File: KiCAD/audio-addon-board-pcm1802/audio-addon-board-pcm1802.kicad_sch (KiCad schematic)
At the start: 68 parts, among them J1 RCA, J2 CONN_HOST_1, J3 RCA, J4 RCA, J5 RCA, SW1 SW_DIP_x04, U1 PCM1802DBR, U2 LTC1682IS8-5, U3 SN74LVC1G125DBV

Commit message: working on layout
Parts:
- added C25: 1uF, Capacitor_SMD:C_0603_1608Metric, symbol Device:C_Small
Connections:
- net +3.3V: now also C25.2
- net GND: now also J1.2 (Ext), J4.2 (Ext), C25.1
- net VINL: now also SW1.7; no longer SW1.8
- net VINR: now also SW1.6; no longer SW1.5
- net at SW1.1: now also C12.2, RA3.1; no longer C20.1
- net at C17.2, RA4.1: now also SW1.4; no longer SW1.3
- net at C21.1: now also SW1.3; no longer SW1.4
- net at RA2.1, RA4.2: now also SW1.5; no longer SW1.6
- net at RA1.1, RA3.2: now also SW1.8; no longer SW1.7
- new net: C20.1, SW1.2

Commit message: working on layout (2025-10-09 sent to jlc)
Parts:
- C1, C10, C15, C22, C3, C5, C6, C9, CNP1: LCSC PN (none) -> C96446
- C11, C13, C14, C16, C2, C7, C8, CNP2: LCSC PN (none) -> C21120
- C12, C17, C23, C24, C25: LCSC PN (none) -> C15849
- C18, C19: LCSC PN (none) -> C14858
- C20, C21: LCSC PN (none) -> C53987
- C4: LCSC PN (none) -> C1588
- FB1: LCSC PN (none) -> C1017
- J1, J3, J4, J5, R12, RBYPASS1, RFMT0, RFMT1, RMODE0, RMODE1, ROSR1: now not fitted
- R1, R2, R22: LCSC PN (none) -> C22936
- R10, R5, R6, R7: LCSC PN (none) -> C23345
- R11, R13, R14, R9, RA1, RA2: LCSC PN (none) -> C21190
- R3, R4, R8, RBYPASS2, RFMT2, RFMT4, RMODE2, RMODE4, ROSR2: LCSC PN (none) -> C21189
- RA3, RA4: LCSC PN (none) -> C25819
- SW1: LCSC PN (none) -> C319050
- TP1: footprint TestPoint:TestPoint_Pad_2.0x2.0mm -> TestPoint:TestPoint_Pad_D1.5mm; now not fitted
- U1: LCSC PN (none) -> C1520787
- U2: LCSC PN (none) -> C676404
- U3: LCSC PN (none) -> C23654
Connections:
- net at C24.2, R13.2, R9.1: now also J2.4 (Pin_4); no longer J2.6 (Pin_6)
- net at C23.2, R11.2, R14.1: now also J2.1 (Pin_1); no longer J2.4 (Pin_4)

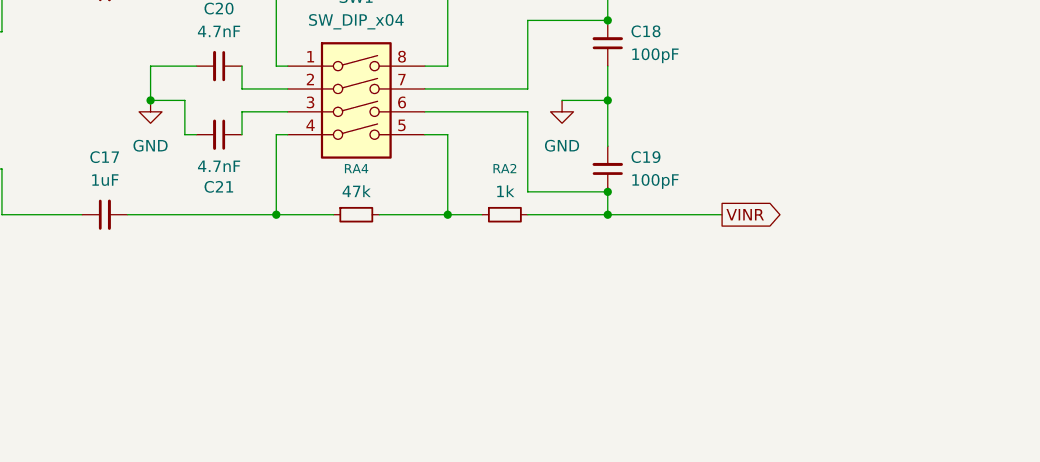
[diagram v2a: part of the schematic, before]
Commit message: add note to fix cap values
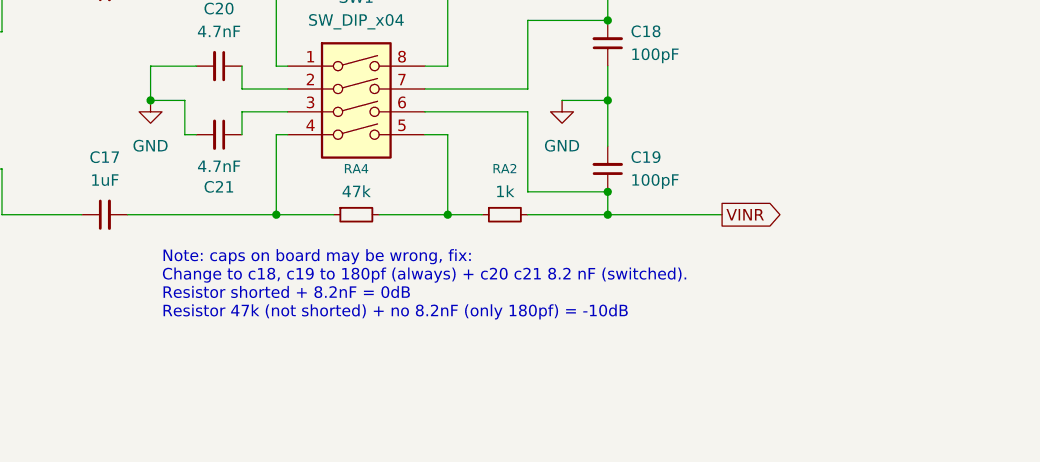
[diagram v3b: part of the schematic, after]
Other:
- note added: "Note: caps on board may be wrong, fix: Change to c18, c19 to 180pf (always) + c20 c21 8.2 nF (switched). Resistor shorted + 8.2nF = 0dB Resistor 47k (not shorted) + no 8.2nF (only 180pf) = -10dB"
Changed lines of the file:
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@@
 	(generator_version "9.0")
 	(paper "A3")
+	(text "Note: caps on board may be wrong, fix:\nChange to c18, c19 to 180pf (always) + c20 c21 8.2 nF (switched).\nResistor shorted + 8.2nF = 0dB\nResistor 47k (not shorted) + no 8.2nF (only 180pf) = -10dB"
+		(exclude_from_sim no)
+		(at 240.03 172.974 0)
+		(effects
+			(font
+				(size 1.27 1.27)
+			)
+			(justify left)
+		)
+	)
 	(text "SCKI, BCK, LRCK, FSYNC, DOUT all 22R"
 		(exclude_from_sim no)
@@
 		(on_board yes)
 		(dnp no)
-		(fields_autoplaced yes)
 		(property "Reference" "C20"
 			(at 246.3736 142.24 90)
@@
 		(on_board yes)
 		(dnp no)
-		(fields_autoplaced yes)
 		(property "Reference" "C17"
 			(at 233.6863 158.75 90)

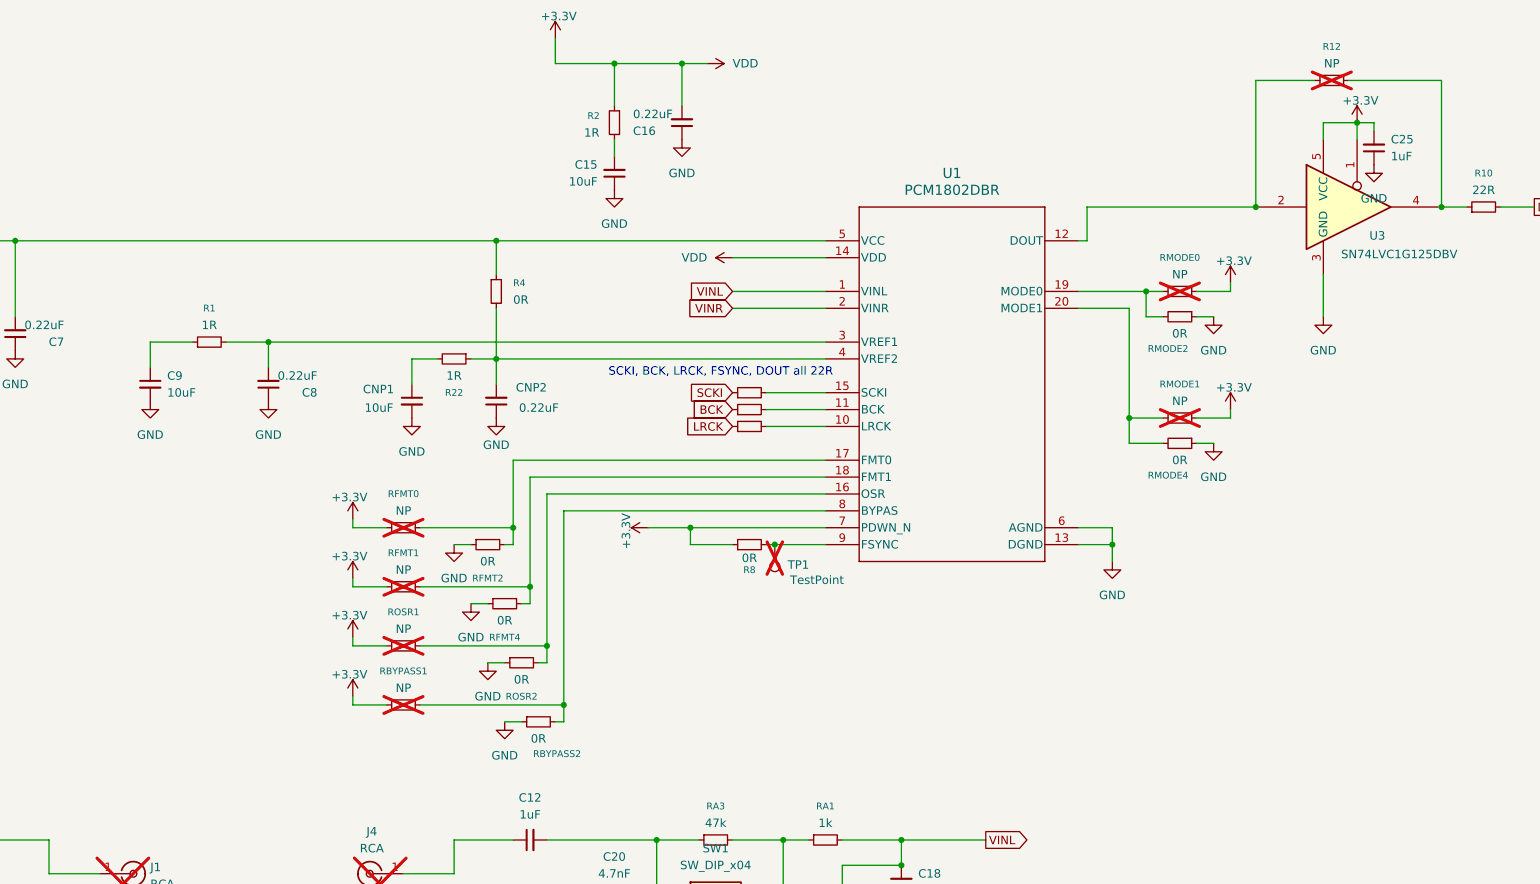
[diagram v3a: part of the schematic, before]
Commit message: update schematic
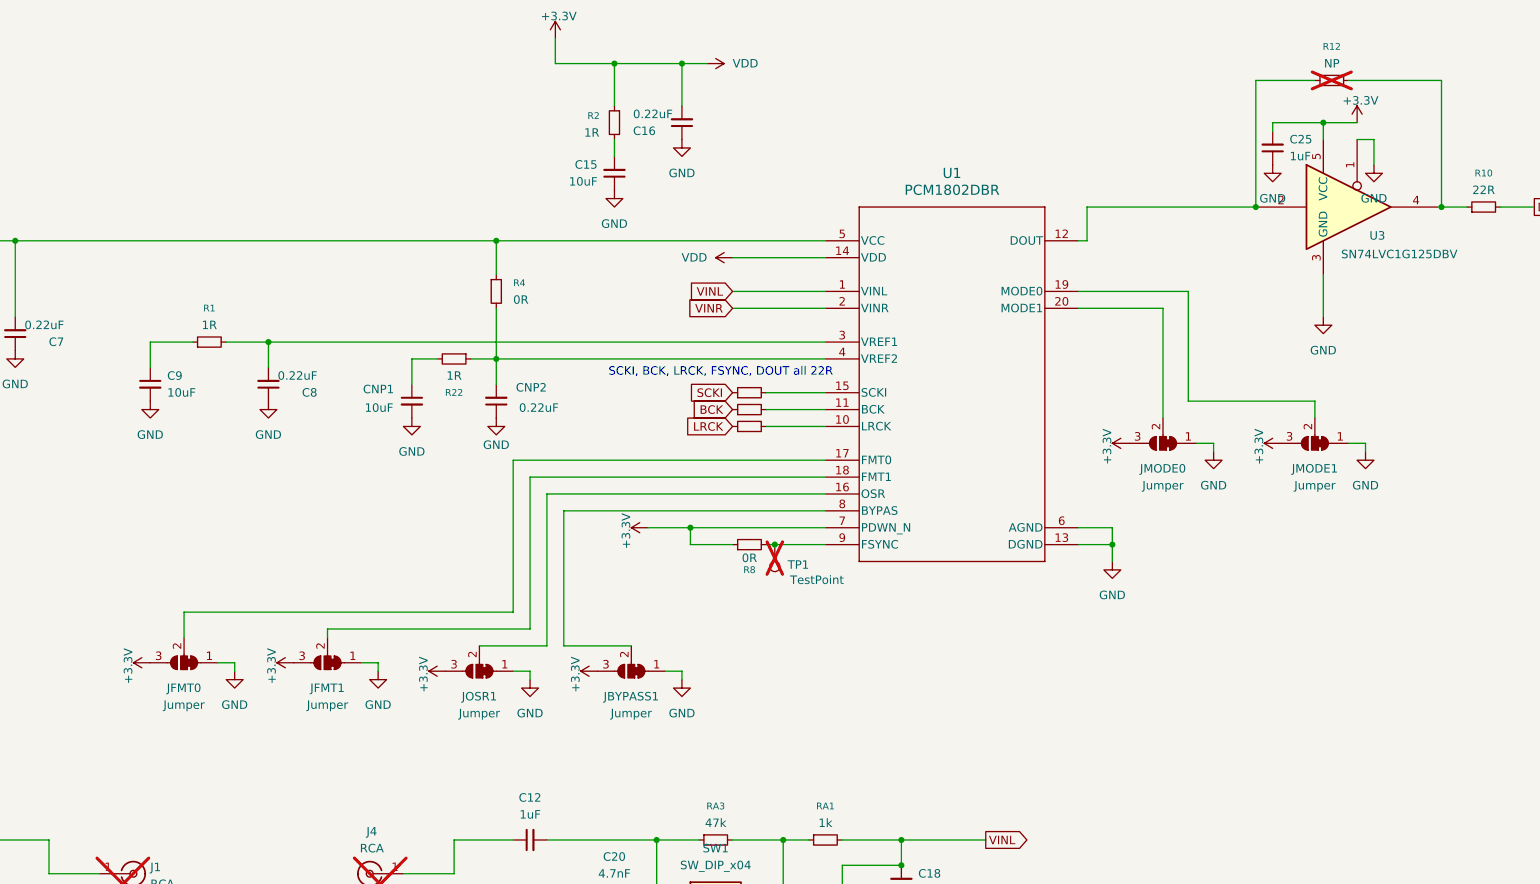
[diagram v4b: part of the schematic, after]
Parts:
- removed RBYPASS1, RFMT0, RFMT1, RMODE0, RMODE1, ROSR1: NP, Resistor_SMD:R_0603_1608Metric, symbol Device:R_Small
- removed RBYPASS2, RFMT2, RFMT4, RMODE2, RMODE4, ROSR2: 0R, Resistor_SMD:R_0603_1608Metric, symbol Device:R_Small
- added JBYPASS1, JFMT0, JMODE0, JMODE1, JOSR1: Jumper, Jumper:SolderJumper-3_P1.3mm_Bridged12_RoundedPad1.0x1.5mm, symbol Jumper:SolderJumper_3_Bridged12
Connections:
- net +3.3V: now also JBYPASS1.3 (B), JFMT0.3 (B), JMODE0.3 (B), JMODE1.3 (B), JOSR1.3 (B); no longer U3.1
- net GND: now also U3.1, JBYPASS1.1 (A), JFMT0.1 (A), JMODE0.1 (A), JMODE1.1 (A), JOSR1.1 (A)
- net at U1.8 (BYPAS): now also JBYPASS1.2 (C)
- net at U1.18 (FMT1): now also JMODE0.2 (C)
- net at U1.17 (FMT0): now also JFMT0.2 (C)
- net at U1.16 (OSR): now also JOSR1.2 (C)
- net at U1.20 (MODE1): now also JMODE0.2 (C)
- net at U1.19 (MODE0): now also JMODE1.2 (C)
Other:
- moved on the sheet: C25

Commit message: initial board fixes
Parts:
- removed R8: 0R, Resistor_SMD:R_0603_1608Metric, symbol Device:R_Small
- removed TP1: TestPoint, TestPoint:TestPoint_Pad_D1.5mm, symbol Connector:TestPoint
- added H1, H2, H3, H4: MountingHole, MountingHole:MountingHole_3.2mm_M3_DIN965_Pad_TopBottom, symbol Mechanical:MountingHole
- added JMODE0: Jumper, Jumper:SolderJumper-3_P1.3mm_Bridged12_RoundedPad1.0x1.5mm, symbol Jumper:SolderJumper_3_Bridged12
- added JP1: Jumper_2_Small_Bridged, Jumper:SolderJumper-2_P1.3mm_Bridged_RoundedPad1.0x1.5mm, symbol Jumper:Jumper_2_Small_Bridged
- renumbered JMODE0 to JFMT1
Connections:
- net +3.3V: now also JMODE0.3 (B), JP1.1 (A)
- net GND: now also JMODE0.1 (A)
- net at U1.20 (MODE1): now also JMODE0.2 (C); no longer JFMT1.2 (C)
- net at U1.9 (FSYNC): now also JP1.2 (B)

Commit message: board fixes, finished
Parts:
- removed C25: 1uF, Capacitor_SMD:C_0603_1608Metric, symbol Device:C_Small
- removed R1, R2, R22: 1R, Resistor_SMD:R_0603_1608Metric, symbol Device:R_Small
- removed R12: NP, Resistor_SMD:R_0603_1608Metric, symbol Device:R_Small
- removed R3: 0R, Resistor_SMD:R_0603_1608Metric, symbol Device:R_Small
- removed U3: SN74LVC1G125DBV, Package_TO_SOT_SMD:SOT-23-5, symbol 74xGxx:SN74LVC1G125DBV
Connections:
- net +3.3V: now also C15.2
- net at CNP2.2, R4.2, U1.4 (VREF2): now also CNP1.1
- net at R10.1: now also U1.12 (DOUT)
- net at C9.1: now also C8.2, U1.3 (VREF1)
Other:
- moved on the sheet: C15, C9, CNP1

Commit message: board fixes, finished
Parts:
- added D1, D2: LED, LED_SMD:LED_0603_1608Metric, symbol Device:LED
- added R1, R2: 1k, Resistor_SMD:R_0603_1608Metric, symbol Device:R_Small
- renumbered JP1 to JFSYNC1
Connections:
- net +3.3V: now also R2.1
- net +5V, Analog: now also R1.1
- net GND: now also D1.1 (K), D2.1 (K)
- new net: D2.2 (A), R2.2
- new net: D1.2 (A), R1.2

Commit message: board fixes
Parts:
- D1, D2: footprint LED_SMD:LED_0603_1608Metric -> LED_SMD:LED_0805_2012Metric
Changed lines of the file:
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@@
 			)
 		)
-		(property "Footprint" "LED_SMD:LED_0603_1608Metric"
+		(property "Footprint" "LED_SMD:LED_0805_2012Metric"
 			(at 224.79 33.02 0)
 			(effects
@@
 			)
 		)
-		(property "Footprint" "LED_SMD:LED_0603_1608Metric"
+		(property "Footprint" "LED_SMD:LED_0805_2012Metric"
 			(at 168.91 62.23 0)
 			(effects
